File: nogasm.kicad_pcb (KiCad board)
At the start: 2 copper layers, 76.2 x 76.2 mm, 59 parts, among them J1 DC Jack PJ-031DH 3.5mm, J2 DC Jack PRT-10811, Q1 BUK92150-55A, Q2 MMBT2222A, Q3 MMBT2222A, Q4 MMBT2222A, U1 WS2812B, U10 WS2812B, U11 WS2812B, U12 WS2812B, U13 WS2812B, U14 WS2812B, U15 LM7805CT, U16 MP3V5050GP, U17 MCP6001 RT-I/OT, U2 WS2812B, U3 WS2812B, U4 WS2812B, U5 Teensy-LC, U6 WS2812B, U7 WS2812B, U8 WS2812B, U9 WS2812B

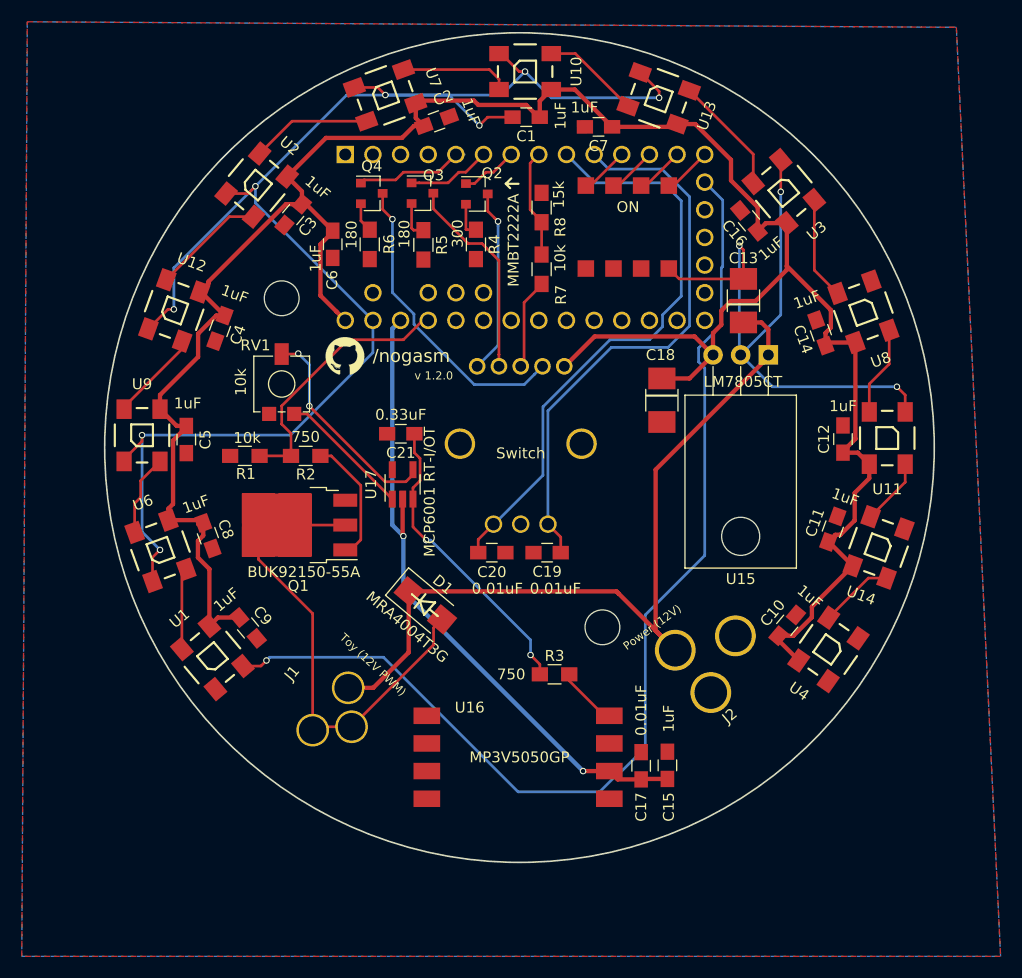
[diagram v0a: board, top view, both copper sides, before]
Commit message: fixing unconnected net and some pcb layout changes
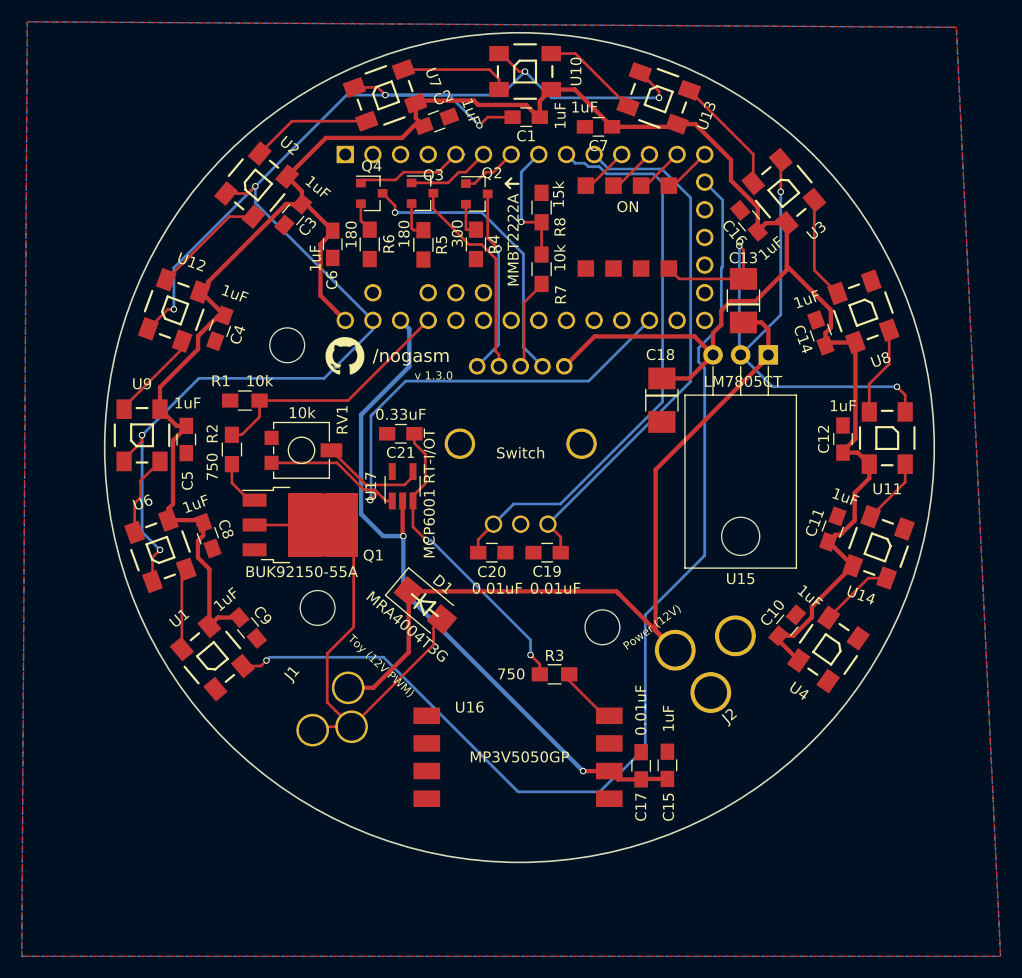
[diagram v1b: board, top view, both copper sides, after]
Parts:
- added REF**: MountingHole_3.2mm_M3, Mounting_Holes:MountingHole_3.2mm_M3, F.Cu at (101.3, 100.1)
- moved R2 6.80 mm to (93.5, 85.5), turned to 90 degrees
- moved RV1 6.36 mm to (99.9, 85.6), turned to 180 degrees
- moved R1 5.08 mm to (94.7, 81.0)
- moved REF** 4.35 mm to (98.6, 75.9)
- moved U17 0.17 mm to (109.2, 88.9)
- moved Q1 0.07 mm to (99.8, 92.5), turned to 0 degrees
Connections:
- RV1 pad 1: /VPRES -> /V_PRES
- U17 pad 1: /VPRES -> /V_PRES
- U5 pad 22: /V_press -> /V_PRES
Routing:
- net /V_PRES: track 0.00 -> 50.7 mm, vias 0 -> 1
- net /VPRES: track 12.7 -> 0.00 mm
- net Net-(RV1-Pad2): track 19.9 -> 10.5 mm, vias 2 -> 0
- net Net-(Q1-Pad1): track 11.7 -> 4.46 mm
- net +3V3: track 61.5 -> 65.7 mm
- net /ENC_B: track 52.0 -> 49.0 mm
- net /ENC_SW: track 10.4 -> 12.1 mm, vias 0 -> 1
- net Net-(Q4-Pad3): track 28.0 -> 26.6 mm
- net GND: track 207.0 -> 205.7 mm
- net Net-(C21-Pad1): track 27.7 -> 28.8 mm
- net /ENC_A: track 54.5 -> 53.4 mm
- net Net-(R1-Pad2): track 25.2 -> 24.4 mm
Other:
- board text added: "v 1.3.0"
- board text removed: "v 1.2.0"

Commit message: layouting LEDs with proper angular distance
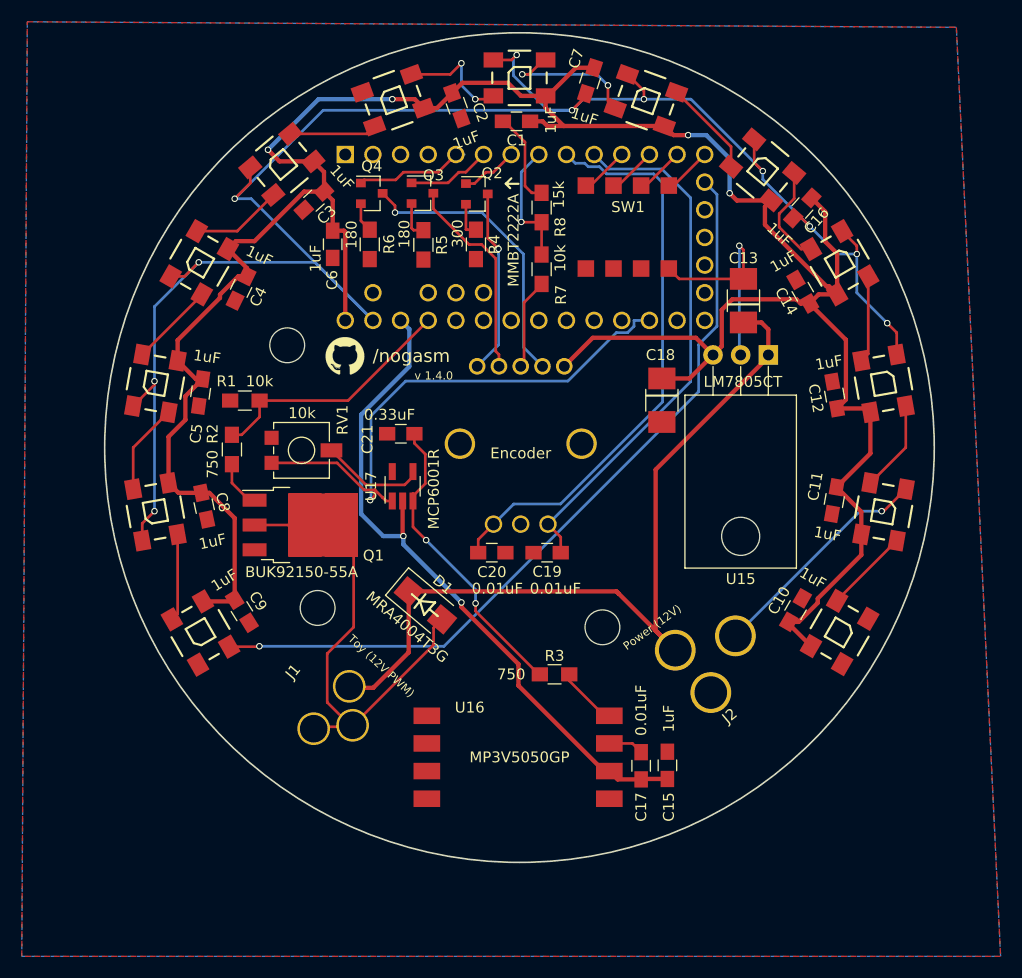
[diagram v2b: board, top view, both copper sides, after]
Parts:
- U17: value MCP6001 RT-I/OT -> MCP6001R
- moved C16 5.04 mm to (145.9, 63.3), turned to 228 degrees
- moved U11 5.03 mm to (153.3, 79.4), turned to 190 degrees
- moved U10 5.01 mm to (149.3, 68.4), turned to 210 degrees
- moved U4 4.95 mm to (90.5, 68.4), turned to 330 degrees
- moved U3 4.92 mm to (86.4, 79.4), turned to 350 degrees
- moved C5 4.51 mm to (90.6, 80.3), turned to 262 degrees
- moved C7 4.31 mm to (126.4, 51.6), turned to 252.1 degrees
- moved C4 4.15 mm to (94.3, 70.7), turned to 244 degrees
- moved C14 4.13 mm to (145.9, 71.0), turned to 120 degrees
- moved C12 4.12 mm to (148.8, 80.5), turned to 100 degrees
- moved U2 3.62 mm to (86.4, 91.2), turned to 10 degrees
- moved U12 3.30 mm to (153.3, 91.2), turned to 170 degrees
- moved U5 2.99 mm to (98.1, 59.3), turned to 310 degrees
- moved U9 2.78 mm to (142.2, 59.8), turned to 230 degrees
- moved C8 2.74 mm to (90.9, 90.7), turned to 282 degrees
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- renumbered Switch to Encoder, ON to SW1, U8 to U10, U14 to U12, U4 to U13, U5 to U14, U6 to U2, U9 to U3, U12 to U4, U2 to U5, U7 to U6, U10 to U7, U13 to U8, U3 to U9
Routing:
- net /5VIO: track 100.1 -> 73.2 mm
- net GND: track 205.7 -> 229.6 mm, vias 11 -> 13
- net +5V: track 224.8 -> 244.2 mm, vias 0 -> 4
- net Net-(U7-Pad2): track 9.05 -> 13.4 mm, vias 0 -> 2
- net Net-(U5-Pad2): track 11.1 -> 8.04 mm
- net Net-(U11-Pad2): track 6.14 -> 8.41 mm
- net Net-(U8-Pad2): track 11.0 -> 8.93 mm
- net Net-(U4-Pad2): track 10.4 -> 8.41 mm
- net +3V3: track 65.7 -> 64.5 mm
- net Net-(U12-Pad2): track 6.82 -> 7.80 mm
- net Net-(U2-Pad2): track 7.49 -> 8.41 mm
- net Net-(U3-Pad2): track 8.46 -> 7.80 mm
- net Net-(U6-Pad2): track 10.1 -> 10.6 mm, vias 0 -> 2
- net Net-(U1-Pad2): track 7.50 -> 8.02 mm
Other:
- board text added: "v 1.4.0"
- board text removed: "v 1.3.0"
